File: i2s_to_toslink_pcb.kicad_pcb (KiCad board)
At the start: 2 copper layers, 61.5 x 61.7 mm, 66 parts, among them J1 PWR IN, J10 FCR684204T, J11 DIN_DOUT_2TP, J12 MCU_GPIOS1, J13 AJ_TP5, J14 C_G0, J15 C_G7, J16 C_RST, J17 C_CLKOUT, J2 EXT_CLK_IN5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

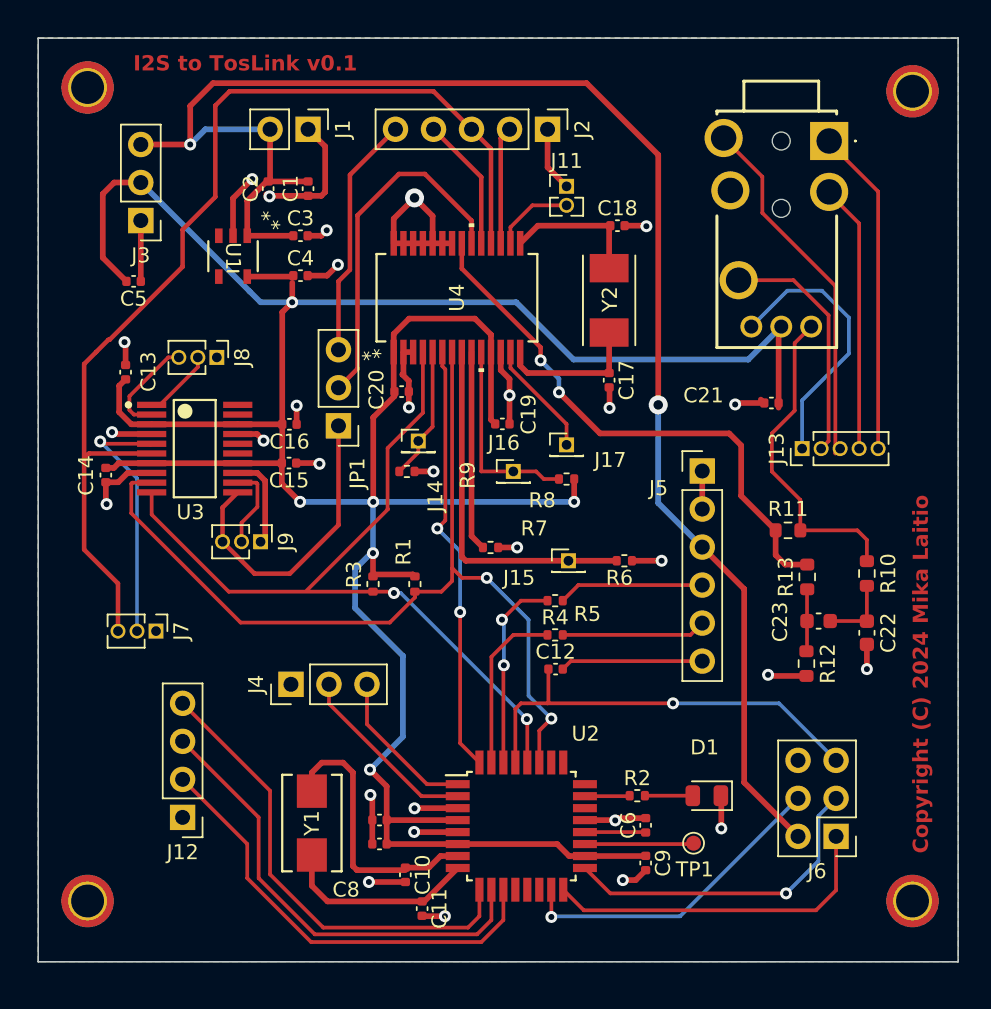
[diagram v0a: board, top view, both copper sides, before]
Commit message: various updates
- removed duplicates 5V power connectors
- now the whole pcb is always powered via 6 pin
  atmega avr isp connector
- added connector for wm8805 rx0 and rx1
- added labels for jumpers/connectors
- moved the orientation of existing connecors
- moved the location of ldo close to
  6 pin avr isp connector

Signed-off-by: Mika Laitio <lamikr@gmail.com>
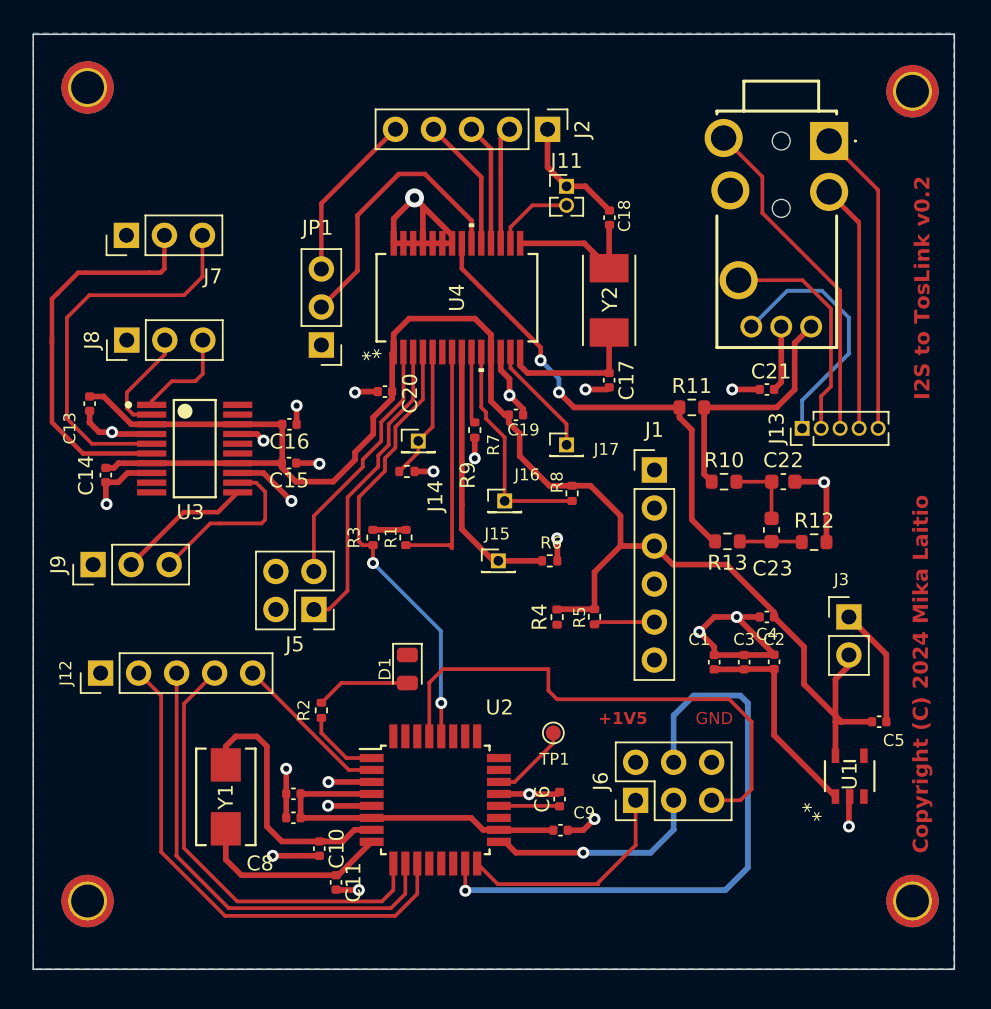
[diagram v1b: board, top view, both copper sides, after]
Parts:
- removed C12: 0u1F, Capacitor_SMD:C_0402_1005Metric
- removed J4: MCU_GPIOS2, Connector_PinHeader_2.54mm:PinHeader_1x03_P2.54mm_Vertical
- C21: value C -> 0u1F
- J1: value PWR IN -> FTDI_6P; footprint Connector_PinHeader_2.54mm:PinHeader_1x02_P2.54mm_Vertical -> Connector_PinHeader_2.54mm:PinHeader_1x06_P2.54mm_Vertical
- J12: value MCU_GPIOS1 -> MCU_GPIOS; footprint Connector_PinHeader_2.54mm:PinHeader_1x04_P2.54mm_Vertical -> Connector_PinHeader_2.54mm:PinHeader_1x05_P2.54mm_Vertical
- J3: footprint Connector_PinHeader_2.54mm:PinHeader_1x03_P2.54mm_Vertical -> Connector_PinHeader_2.54mm:PinHeader_1x02_P2.54mm_Vertical
- J5: value FTDI_6P -> RX0/RX1; footprint Connector_PinHeader_2.54mm:PinHeader_1x06_P2.54mm_Vertical -> Connector_PinHeader_2.54mm:PinHeader_2x02_P2.54mm_Vertical
- J7, J8, J9: footprint Connector_PinHeader_1.27mm:PinHeader_1x03_P1.27mm_Vertical -> Connector_PinHeader_2.54mm:PinHeader_1x03_P2.54mm_Vertical
- R4: value 0k -> 1k
- R5: value 10k -> 1k
- U1: value PTLV709A33DBVR -> TLV709A33DBVR
- moved C5 57.9 mm to (77.0, 66.0)
- moved J3 54.2 mm to (75.0, 59.0), turned to 0 degrees
- moved U1 53.9 mm to (75.0, 69.6), turned to 90 degrees
- moved C2 46.3 mm to (70.0, 62.0)
- moved C1 41.7 mm to (66.0, 62.0)
- moved C3 41.1 mm to (68.0, 62.0), turned to 90 degrees
- moved C4 38.6 mm to (69.5, 59.0), turned to 180 degrees
- moved J1 32.5 mm to (62.0, 49.2), turned to 0 degrees
- moved J5 27.5 mm to (39.2, 58.5), turned to 180 degrees
- moved J7 26.5 mm to (26.7, 33.5), turned to 90 degrees
- moved R2 21.9 mm to (39.8, 65.2), turned to 90 degrees
- moved D1 21.7 mm to (45.5, 62.5), turned to -90 degrees
- moved J6 13.6 mm to (60.8, 71.2), turned to 90 degrees
- moved TP1 11.9 mm to (55.2, 66.8)
- moved C22 11.5 mm to (70.6, 50.0), turned to 0 degrees
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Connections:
- C1 pad 1: GND -> VIN_5V
- C1 pad 2: VIN_5V -> GND
- C2 pad 1: GND -> VIN_5V
- C2 pad 2: VIN_5V -> GND
- J1 pad 2: VIN_5V -> GND
- J5 pad 1: GND -> Net-(J5-Pin_1)
- J5 pad 3: VIN_5V -> Net-(J5-Pin_3)
- J5 pad 4: Net-(J5-Pin_4) -> GND
- J7 pad 2: Net-(J7-Pin_2) -> EXTERNAL_IN_I2S_BCLK
- J7 pad 3: EXTERNAL_IN_I2S_BCLK -> Net-(J7-Pin_3)
- J9 pad 2: Net-(J9-Pin_2) -> CLKGEN_OUT_I2S_MCLK
- J9 pad 3: CLKGEN_OUT_I2S_MCLK -> Net-(J9-Pin_3)
- R4 pad 1: MCU_TXD0 -> MCU_RXD0
- R4 pad 2: Net-(J5-Pin_5) -> VCC_3V3
- R5 pad 1: MCU_RXD0 -> VCC_3V3
- R5 pad 2: Net-(J5-Pin_4) -> MCU_TXD0
- TP1 pad 1: Net-(U2-ADC6) -> Net-(U2-ADC7)
- U2 pad 1: Net-(J4-Pin_3) -> MCU_LED
- U2 pad 19: Net-(U2-ADC6) -> unconnected-(U2-ADC6-Pad19)
- U2 pad 2: Net-(J4-Pin_2) -> Net-(J12-Pin_5)
- U2 pad 22: unconnected-(U2-ADC7-Pad22) -> Net-(U2-ADC7)
- U2 pad 23: MCU_LED -> unconnected-(U2-PC0-Pad23)
- U3 pad 1: Net-(J8-Pin_2) -> Net-(J8-Pin_3)
- U3 pad 12: Net-(J9-Pin_2) -> Net-(J9-Pin_3)
- U3 pad 2: Net-(J8-Pin_3) -> Net-(J8-Pin_2)
- U3 pad 5: Net-(J7-Pin_2) -> Net-(J7-Pin_3)
- U4 pad 2: GND -> Net-(J5-Pin_3)
- U4 pad 3: GND -> Net-(J5-Pin_1)
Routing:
- net VIN_5V: track 108.7 -> 13.9 mm, vias 2 -> 0
- net VCC_3V3: track 205.7 -> 138.6 mm, vias 6 -> 0
- net MCU_SDA1: track 61.5 -> 16.3 mm, vias 2 -> 0
- net EXTERNAL_IN_I2S_BCLK: track 71.1 -> 35.0 mm
- net MCU_INT0: track 28.9 -> 0.00 mm, vias 2 -> 0
- net Net-(J7-Pin_3): track 0.00 -> 26.1 mm
- net MCU_SCL1: track 54.5 -> 30.1 mm
- net Net-(J5-Pin_1): track 0.00 -> 20.5 mm
- net MCU_MOSI: track 21.8 -> 41.2 mm
- net Net-(J7-Pin_2): track 17.3 -> 0.00 mm, vias 1 -> 0
- net Net-(J5-Pin_3): track 0.00 -> 17.1 mm
- net MCU_RXD0: track 13.2 -> 0.00 mm, vias 2 -> 0
- net Net-(J4-Pin_2): track 12.5 -> 0.00 mm
- net Net-(J9-Pin_3): track 0.00 -> 11.6 mm
- net CLKGEN_OUT_I2S_MCLK: track 20.3 -> 9.12 mm
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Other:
- board size 61.5 x 61.7 mm -> 61.5 x 62.5 mm
- board text added: "+1V5"
- board text added: "GND"
- board text added: "I2S to TosLink v0.2"
- board text removed: "I2S to TosLink v0.1"

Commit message: finished v0.2 design
- mcu ftdi serial connector reset pin
  to 3v3 instead of 5v
- 3.3v pull-up resistor, cap and diode for mcu reset
- mcu reset button
- solder paste clearance -20% for
  mcu, codec, clk gen and ldo to help
  spreading pasta to small pins close to
  ech others

Signed-off-by: Mika Laitio <lamikr@gmail.com>
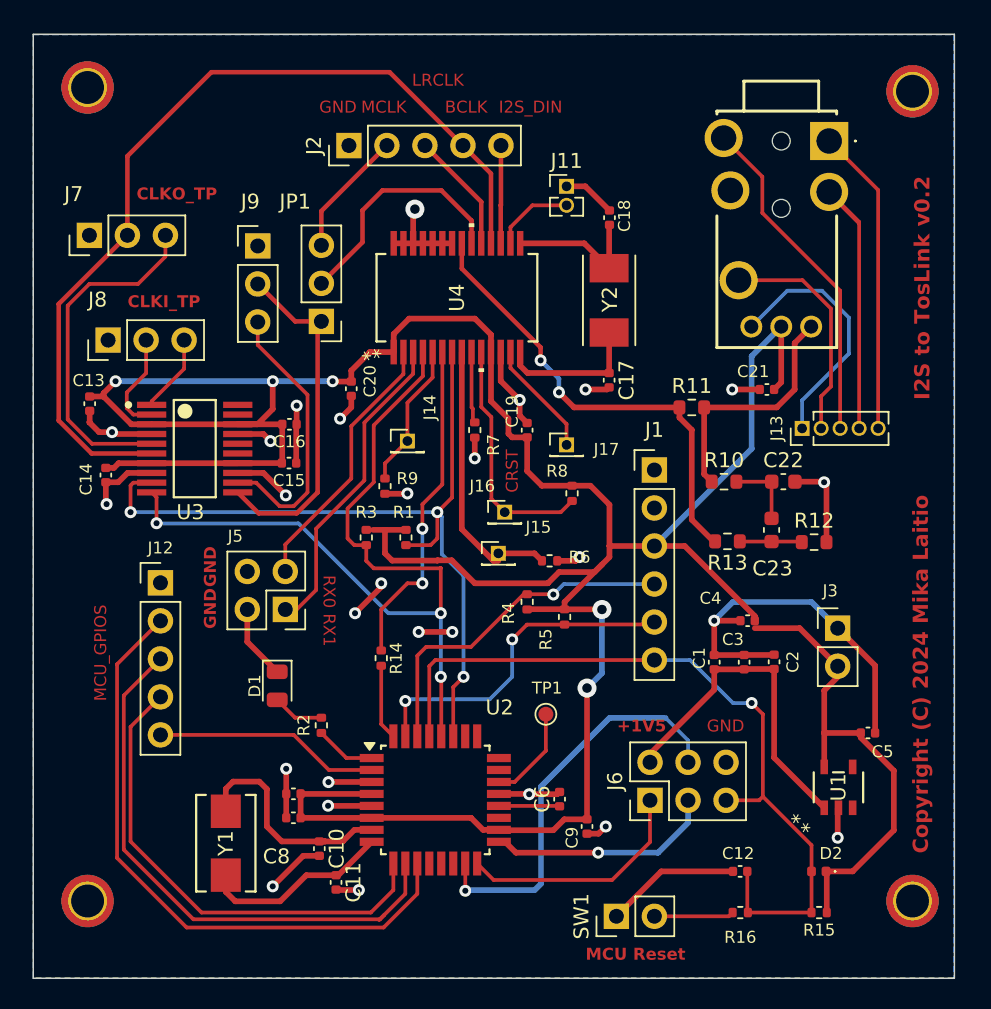
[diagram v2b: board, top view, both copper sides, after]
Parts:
- added C12: 100nF, Capacitor_SMD:C_0402_1005Metric, F.Cu at (67.7, 76.0)
- added D2: D, Diode_SMD:D_0402_1005Metric, F.Cu at (73.0, 76.0)
- added R14: 0k, Resistor_SMD:R_0402_1005Metric, F.Cu at (43.8, 61.8)
- added R15: 4k7, Resistor_SMD:R_0402_1005Metric, F.Cu at (73.0, 78.8)
- added R16: 330, Resistor_SMD:R_0402_1005Metric, F.Cu at (67.7, 78.8)
- added SW1: SW_Push, Connector_PinHeader_2.54mm:PinHeader_1x02_P2.54mm_Vertical, F.Cu at (59.5, 79.0)
- J16: value C_RST -> CRST
- moved J9 24.0 mm to (35.5, 34.2), turned to 0 degrees
- moved J2 13.3 mm to (41.6, 27.5), turned to 90 degrees
- moved D1 8.77 mm to (36.8, 63.6)
- moved J12 7.24 mm to (29.0, 56.7), turned to 0 degrees
- moved Y1 3.10 mm to (33.4, 74.1)
- moved J7 2.48 mm to (24.2, 33.5)
- moved C20 2.26 mm to (41.8, 43.8), turned to 90 degrees
- moved R4 2.25 mm to (53.5, 58.0), turned to -90 degrees
- moved R5 2.00 mm to (56.0, 59.0)
- moved J5 1.91 mm to (37.3, 58.5)
- moved C9 1.79 mm to (57.5, 73.0), turned to -90 degrees
- moved R9 1.77 mm to (44.0, 50.3), turned to -90 degrees
- moved JP1 1.58 mm to (39.8, 39.2)
- moved TP1 1.35 mm to (54.8, 65.5)
- moved C4 1.31 mm to (68.2, 59.2)
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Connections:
- J2 pad 2: EXTERNAL_IN_I2S_DIN -> EXTERNAL_IN_I2S_MCLK
- J2 pad 3: EXTERNAL_IN_I2S_BCLK -> EXTERNAL_IN_I2S_LRCLK
- J2 pad 4: EXTERNAL_IN_I2S_LRCLK -> EXTERNAL_IN_I2S_BCLK
- J2 pad 5: EXTERNAL_IN_I2S_MCLK -> EXTERNAL_IN_I2S_DIN
- U4 pad 6: MCU_INT0 -> CODEC_INT0
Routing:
- net VCC_3V3: track 138.6 -> 218.9 mm, vias 0 -> 5
- net MCU_SDA1: track 16.3 -> 54.9 mm, vias 0 -> 3
- net MCU_SCL1: track 30.1 -> 57.2 mm, vias 2 -> 3
- net EXTERNAL_IN_I2S_BCLK: track 35.0 -> 60.8 mm
- net MCU_RXD0: track 0.00 -> 23.2 mm, vias 0 -> 1
- net CODEC_INT0: track 0.00 -> 22.2 mm, vias 0 -> 2
- net MCU_TXD0: track 4.07 -> 22.4 mm, vias 0 -> 2
- net MCU_RST: track 35.3 -> 52.8 mm, vias 0 -> 1
- net CLKGEN_OUT_I2S_MCLK: track 9.12 -> 23.0 mm
- net MCU_MOSI: track 41.2 -> 27.4 mm
- net GND: track 105.1 -> 117.7 mm, vias 25 -> 27
- net Net-(J12-Pin_2): track 34.1 -> 42.0 mm
- net VIN_5V: track 13.9 -> 21.8 mm
- net Net-(J9-Pin_3): track 11.6 -> 18.5 mm
- net Net-(J12-Pin_3): track 31.4 -> 37.7 mm
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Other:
- board size 61.5 x 62.5 mm -> 61.5 x 63.1 mm
- board text added: "BCLK"
- board text added: "CLKI_TP"
- board text added: "CLKO_TP"
- board text added: "I2S_DIN"
- board text added: "LRCLK"
- board text added: "MCLK"
- board text added: "MCU Reset"
- board text added: "RX0 RX1"

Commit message: inceased the size of some tp headers to 2.00mm
Signed-off-by: Mika Laitio <lamikr@gmail.com>
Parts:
- J11: footprint Connector_PinHeader_1.27mm:PinHeader_1x02_P1.27mm_Vertical -> Connector_PinHeader_2.00mm:PinHeader_1x02_P2.00mm_Vertical
- J13: footprint Connector_PinHeader_1.27mm:PinHeader_1x05_P1.27mm_Vertical -> Connector_PinHeader_2.00mm:PinHeader_1x05_P2.00mm_Vertical
- moved J11 2.24 mm to (56.4, 28.0)
- moved J13 0.33 mm to (72.2, 46.4)
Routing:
- net GND: track 117.7 -> 120.0 mm
- net Net-(J10-RIGHT_CHANNEL): track 19.6 -> 17.7 mm
- net Net-(J11-Pin_2): track 5.43 -> 7.11 mm
- net Net-(J10-DETECTOR_1): track 20.6 -> 21.9 mm
- net Net-(J10-DETECTOR_2): track 22.6 -> 23.4 mm
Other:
- board size 61.5 x 63.1 mm -> 61.9 x 63.1 mm

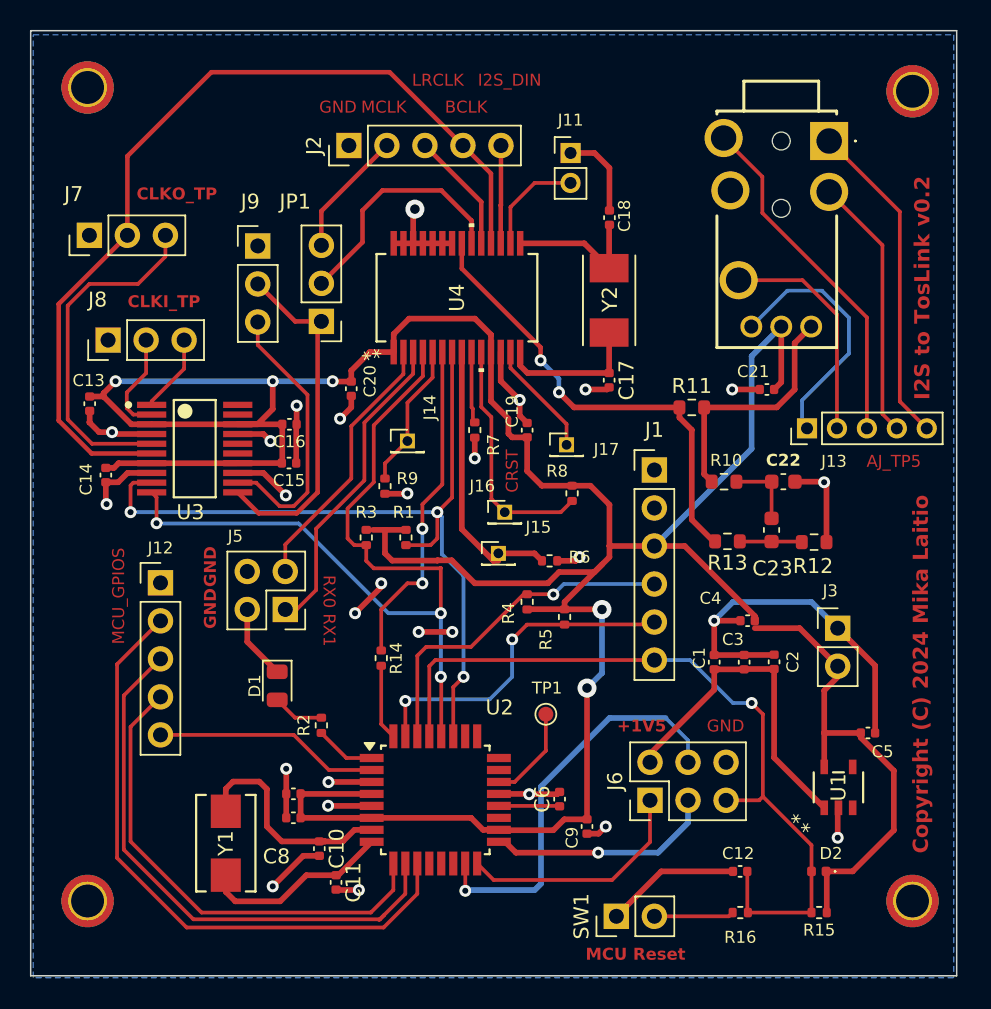
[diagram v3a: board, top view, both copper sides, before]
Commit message: component footprint updates
- 0402 caps and resistors to 0603
- reset pin-header to reset button

Signed-off-by: Mika Laitio <lamikr@gmail.com>
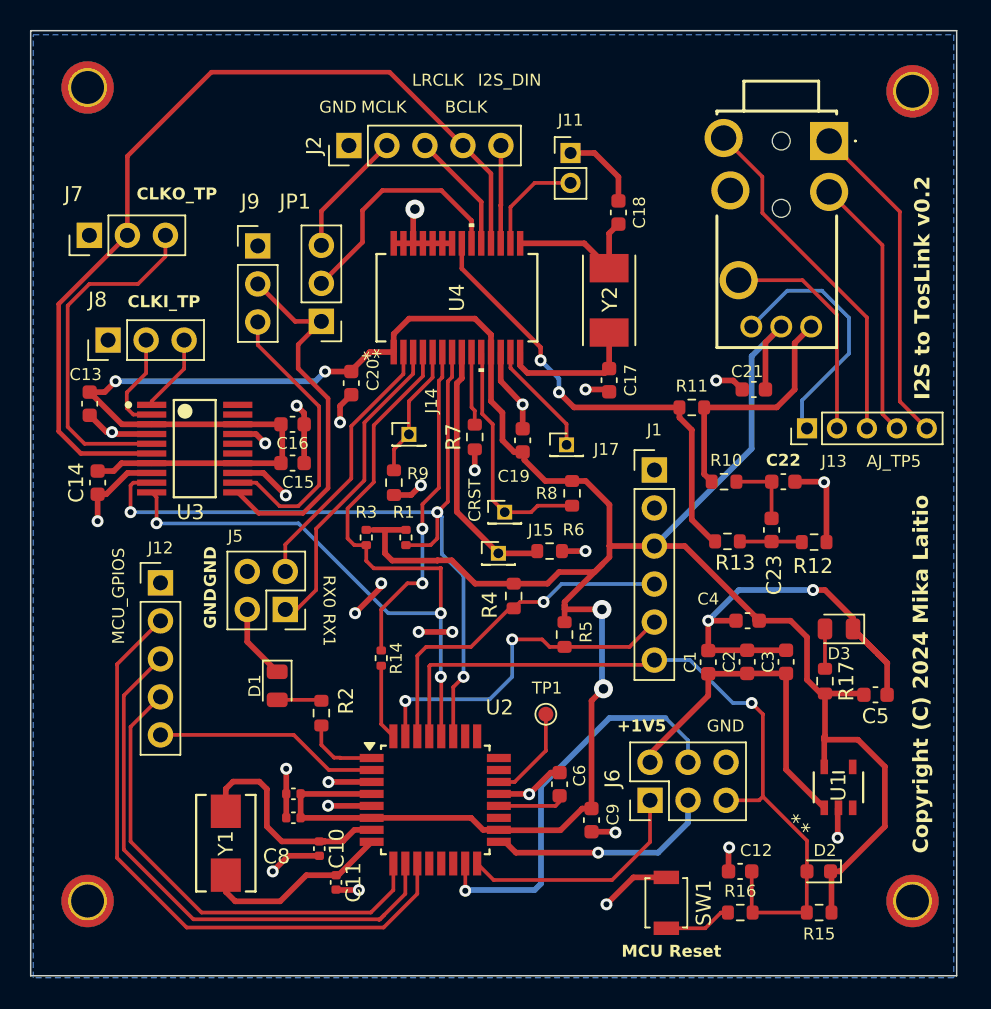
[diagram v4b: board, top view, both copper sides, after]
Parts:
- removed J3: PWR Test, Connector_PinHeader_2.54mm:PinHeader_1x02_P2.54mm_Vertical
- added D3: LED, LED_SMD:LED_0805_2012Metric, F.Cu at (74.3, 59.8)
- added R17: 1K5, Resistor_SMD:R_0603_1608Metric, F.Cu at (73.4, 63.3)
- C1, C12, C13, C14, C15, C16, C17, C18, C19, C2, C20, C21, C3, C4, C5, C6, C9: footprint Capacitor_SMD:C_0402_1005Metric -> Capacitor_SMD:C_0603_1608Metric
- D2: footprint Diode_SMD:D_0402_1005Metric -> Diode_SMD:D_0603_1608Metric
- R15, R16, R2, R4, R5, R6, R7, R8, R9: footprint Resistor_SMD:R_0402_1005Metric -> Resistor_SMD:R_0603_1608Metric
- SW1: footprint Connector_PinHeader_2.54mm:PinHeader_1x02_P2.54mm_Vertical -> Button_Switch_SMD:SW_SPST_B3U-1000P
- moved SW1 3.46 mm to (62.8, 78.1), turned to -90 degrees
- moved C3 2.80 mm to (70.8, 62.0)
- moved C5 2.60 mm to (76.8, 64.2)
- moved C2 1.80 mm to (68.2, 62.0)
- moved R5 1.17 mm to (56.0, 60.2)
- moved C6 1.00 mm to (55.7, 70.2)
- moved R4 0.98 mm to (52.6, 57.6), turned to 90 degrees
- moved C21 0.87 mm to (68.6, 43.8)
- moved R2 0.81 mm to (39.8, 65.4)
- moved C14 0.75 mm to (24.8, 50.0)
- moved C19 0.74 mm to (53.2, 47.2)
- moved C18 0.69 mm to (59.6, 32.0)
- moved R6 0.65 mm to (55.0, 54.6)
- moved R9 0.64 mm to (44.6, 50.0)
- moved C9 0.52 mm to (57.8, 72.6)
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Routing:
- net VCC_3V3: track 218.8 -> 213.2 mm, vias 5 -> 4
- net GND: track 120.0 -> 123.0 mm, vias 27 -> 30
- net Net-(D3-A): track 0.00 -> 2.67 mm
- net CLKGEN_OUT_I2S_MCLK: track 23.0 -> 25.2 mm
- net MCU_RST: track 52.8 -> 51.5 mm
- net CODEC_GPO7: track 18.3 -> 17.2 mm
- net MCU_LED: track 4.05 -> 5.02 mm
- net Net-(J9-Pin_3): track 18.5 -> 19.3 mm
- net CODEC_GPO0: track 9.77 -> 8.97 mm
- net Net-(R16-Pad1): track 5.33 -> 4.55 mm
- net MCU_TXD0: track 22.4 -> 23.1 mm
- net Net-(D1-A): track 3.44 -> 2.89 mm
